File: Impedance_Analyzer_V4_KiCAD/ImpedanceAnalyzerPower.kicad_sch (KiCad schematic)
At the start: 42 parts, among them J8 Barrel_Jack_Switch, J9 USB_B_Micro, U1 AD8022, U2 AD8022, U5 L7805

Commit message: v4
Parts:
- removed C4, C6: 22u, Capacitor_THT:CP_Radial_D5.0mm_P2.00mm, symbol Device:CP
- removed C7, C9: CP, Capacitor_THT:CP_Radial_D8.0mm_P5.00mm, symbol Device:CP
- removed D1: D, Diode_SMD:D_SMA, symbol Device:D
- removed D4, D5: LED, LED_SMD:LED_1206_3216Metric, symbol Device:LED
- removed J8: Barrel_Jack_Switch, Connector_BarrelJack:BarrelJack_Horizontal, symbol Connector:Barrel_Jack_Switch
- removed J9: USB_B_Micro, Connector_USB:USB_Micro-B_Wuerth_629105150521, symbol Connector:USB_B_Micro
- removed R19, R20: 1k, Resistor_SMD:R_1206_3216Metric, symbol Device:R
- removed Reg1: DPUN02L-XX, Martinos:SIP-2W-7, symbol Martinos:DPUN02L-XX
- removed U5: L7805, Package_TO_SOT_THT:TO-220-3_Vertical, symbol Regulator_Linear:L7805
- added C27, C28, C29: 1000u, Capacitor_SMD:CP_Elec_10x10.5, symbol Device:CP
- added C4, C6: 1500p, Capacitor_SMD:C_0805_2012Metric, symbol Device:C
- added D4, D5: 1N5819WS, Diode_SMD:D_SOD-323, symbol Diode:1N5819WS
- added F1: 1A, Fuse:Fuse_1206_3216Metric_Pad1.42x1.75mm_HandSolder, symbol Device:Polyfuse
- added J2: USB_B_Micro, Connector_USB:USB_Micro-B_Wuerth_629105150521, symbol Connector:USB_B_Micro
- added J3, J8: Conn_01x02_Male, Connector_PinHeader_2.54mm:PinHeader_1x02_P2.54mm_Vertical, symbol Connector:Conn_01x02_Male
- added L3, L4: 10u, Inductor_SMD:L_Taiyo-Yuden_NR-60xx_HandSoldering, symbol Device:L
- added R11, R4: 8.2k, Resistor_SMD:R_1206_3216Metric, symbol Device:R
- added R12, R5: 0.24, Resistor_SMD:R_1206_3216Metric, symbol Device:R
- added R13, R6: 953, Resistor_SMD:R_1206_3216Metric, symbol Device:R
- added R15: 180, Resistor_SMD:R_1206_3216Metric, symbol Device:R
- added TP1, TP2: TestPoint, TestPoint:TestPoint_Plated_Hole_D3.0mm, symbol Connector:TestPoint
- added U5, U8: MC34063AD, Package_SO:SOIC-8_3.9x4.9mm_P1.27mm, symbol Regulator_Switching:MC34063AD
- L1, L2: value 10u -> 100u; footprint Inductor_SMD:L_Taiyo-Yuden_NR-60xx_HandSoldering -> Inductor_SMD:L_Taiyo-Yuden_NR-80xx_HandSoldering
- U1, U2: value AD8022 -> ADA4075-2; symbol Amplifier_Operational:LM358 -> Amplifier_Operational:ADA4075-2
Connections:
- net +5V: now also C5.1, C29.1, F1.2, R12.1, R5.1, U5.6 (Vin), U8.6 (Vin)
- net GND: now also L1.2, C27.1, C28.2, C29.2, C6.2, J2.5 (GND), J2.6 (Shield), R11.1, R4.1, U8.2 (SwE), U8.4 (GND)
- net at L2.2: now also D5.2 (A), U8.1 (SwC)
- net +5VP renamed +12V
- net +12V: now also L4.2, TP2.1; no longer L1.1
- net -5V renamed -12V
- net -12V: now also L3.2, TP1.1; no longer L2.1
- new net: R11.2, R13.1, U8.5 (Vfb)
- new net: J2.1 (VBUS), J3.1 (Pin_1)
- new net: F1.1, J3.2 (Pin_2), J8.1 (Pin_1)
- new net: D4.1 (K), L1.1, U5.2 (SwE)
- new net: L2.1, R12.2, R15.2, U8.7 (Ipk)
- new net: C27.2, C4.2, D4.2 (A), L3.1, R6.2, U5.4 (GND)
- new net: R4.2, R6.1, U5.5 (Vfb)
- new net: R15.1, U8.8 (DC)
- new net: C6.1, U8.3 (TC)
- new net: C28.1, D5.1 (K), L4.1, R13.2
- new net: J2.2 (D-), J2.3 (D+), J2.4 (ID)
- new net: C4.1, U5.3 (TC)
- new net: R5.2, U5.1 (SwC), U5.7 (Ipk), U5.8 (DC)
- new net +5V-3: J8.2 (Pin_2)
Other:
- moved on the sheet: C19, C20, C26, C3, D6, U1C, U2C

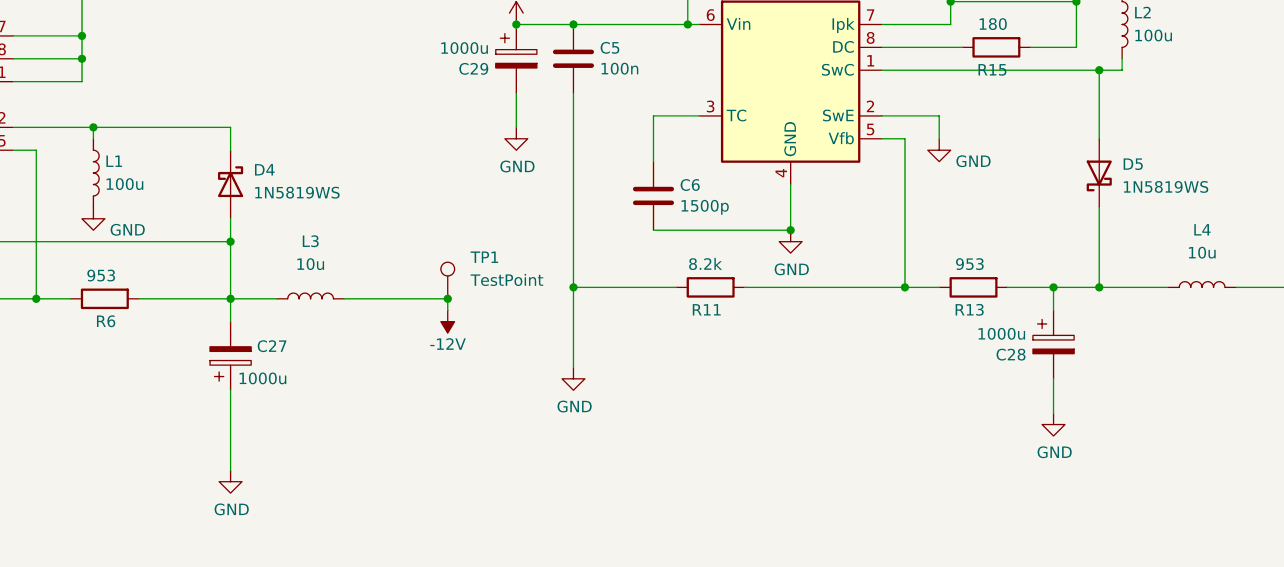
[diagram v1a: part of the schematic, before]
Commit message: Initial Labview update
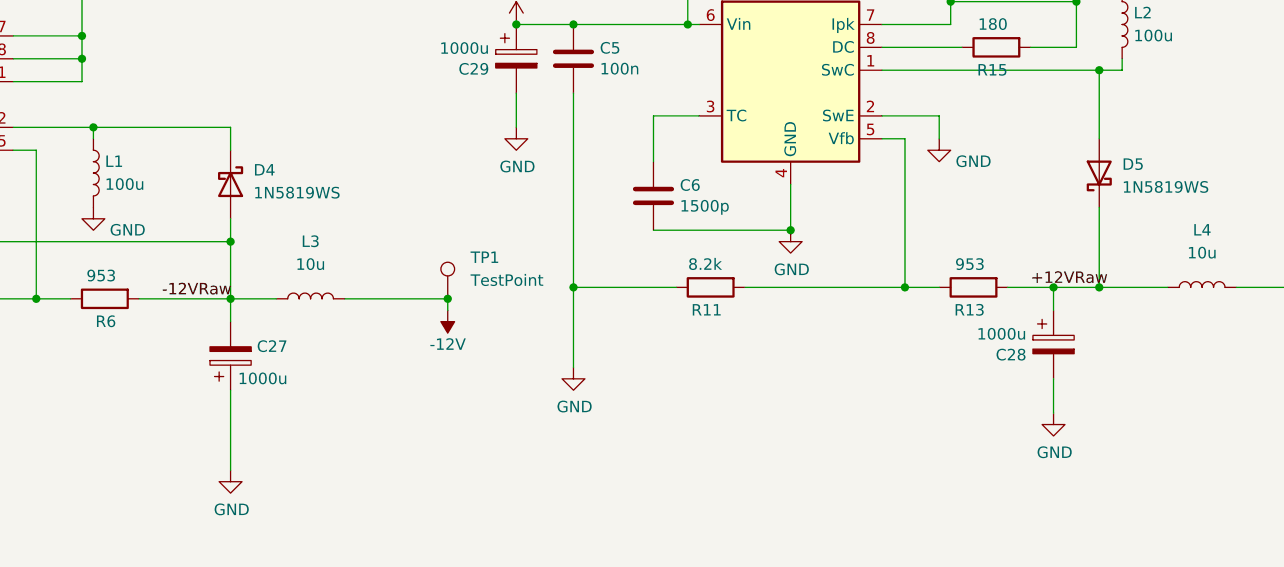
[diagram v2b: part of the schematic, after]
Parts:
- J2: footprint Connector_USB:USB_Micro-B_Wuerth_629105150521 -> Eli_Lib:AMPHENOL_10118194-0001LF
- TP1, TP2: footprint TestPoint:TestPoint_Plated_Hole_D3.0mm -> TestPoint:TestPoint_THTPad_2.0x2.0mm_Drill1.0mm
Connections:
- net -12VRaw: now reaches C27.2, C4.2, D4.2 (A), L3.1, R6.2, U5.4 (GND)
- net +12VRaw: now reaches C28.1, D5.1 (K), L4.1, R13.2
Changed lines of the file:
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@@
     (stroke (width 0) (type default) (color 0 0 0 0))
+  )
+  (label "-12VRaw" (at 74.93 142.24 0)
+    (effects (font (size 1.27 1.27)) (justify left bottom))
+  )
+  (label "+12VRaw" (at 171.45 140.97 0)
+    (effects (font (size 1.27 1.27)) (justify left bottom))
   )
   (global_label "+5V-3" (shape input) (at 48.26 69.85 180) (fields_autoplaced)
@@
       (effects (font (size 1.27 1.27)) (justify left))
     )
-    (property "Footprint" "TestPoint:TestPoint_Plated_Hole_D3.0mm" (id 2) (at 111.76 142.24 0)
+    (property "Footprint" "TestPoint:TestPoint_THTPad_2.0x2.0mm_Drill1.0mm" (id 2) (at 111.76 142.24 0)
       (effects (font (size 1.27 1.27)) hide)
     )
@@
     (property "Reference" "J2" (id 0) (at 35.7378 75.7682 0))
     (property "Value" "USB_B_Micro" (id 1) (at 35.7378 78.0796 0))
-    (property "Footprint" "Connector_USB:USB_Micro-B_Wuerth_629105150521" (id 2) (at 38.1 88.9 0)
+    (property "Footprint" "Eli_Lib:AMPHENOL_10118194-0001LF" (id 2) (at 38.1 88.9 0)
       (effects (font (size 1.27 1.27)) hide)
     )
@@
       (effects (font (size 1.27 1.27)) (justify left))
     )
-    (property "Footprint" "TestPoint:TestPoint_Plated_Hole_D3.0mm" (id 2) (at 217.17 140.97 0)
-      (effects (font (size 1.27 1.27)) hide)
-    )
+    (property "Footprint" "TestPoint:TestPoint_THTPad_2.0x2.0mm_Drill1.0mm" (id 2) (at 217.17 140.97 0)
+      (effects (font (size 1.27 1.27)) hide)
+    )
